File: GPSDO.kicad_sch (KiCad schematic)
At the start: 100 parts, among them J1 Conn_Coaxial, J10 Conn_Coaxial, J2 Barrel_Jack, J3 PROG, J4 DISP_MODULE, J5 GPS_CONN, J6 Conn_Coaxial, J7 Conn_Coaxial, J8 Conn_Coaxial, J9 Conn_Coaxial, SW1 RESET_BTN, U1 REF3450, U10 AVR32DB28x-xSO, U11 AZ1117H-5.0TRG1, U12 AZ1117H-5.0TRG1, U13 74HC390, U14 DS34C87T, U15 MCP6486T-E/OT, U2 74AUC2G04, U3 74AUC2G04, U4 74AUC1G74, U5 AD5680, U6 NB3N551MN, U7 74LVC1G125SE-7, U8 74LVC1G125SE-7, U9 LTC2050IS8, X1 OC5SC25

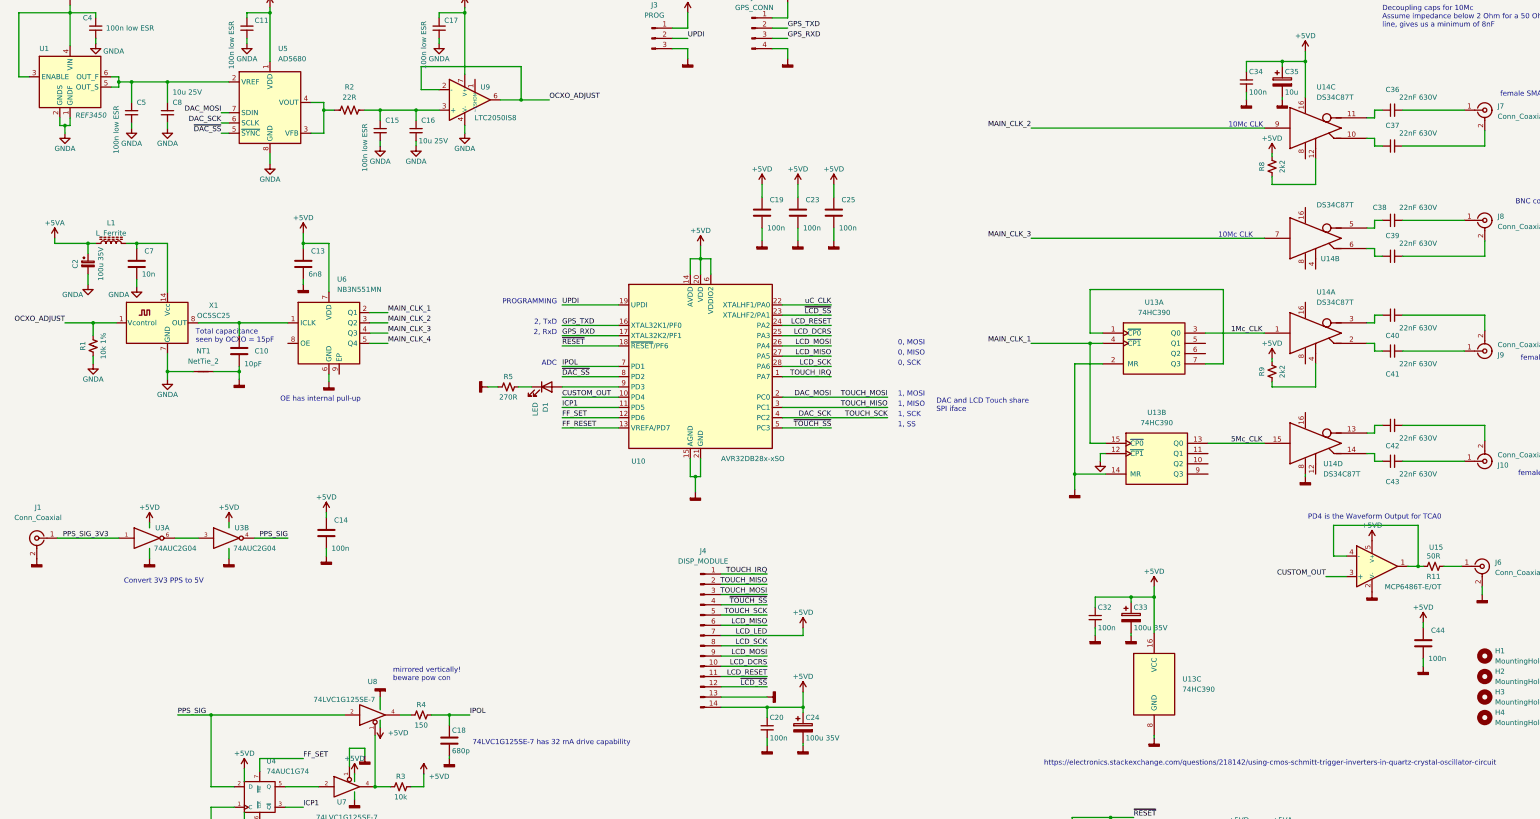
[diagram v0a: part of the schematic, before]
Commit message: Corrected schematic: VREF
VREF was chosen as 5V instead of 4.096V - corrected with REF3440IDBVR
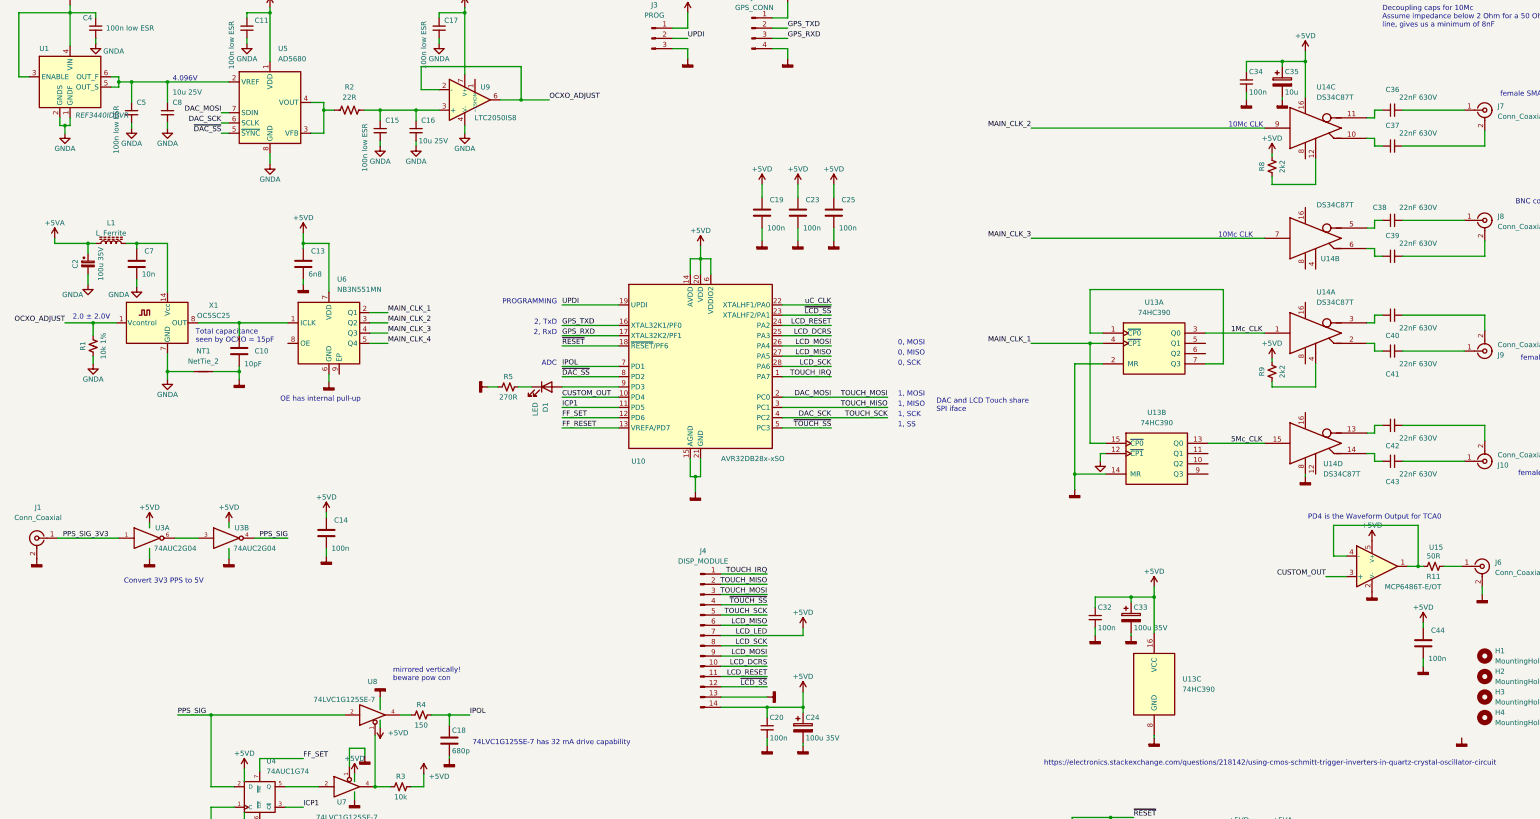
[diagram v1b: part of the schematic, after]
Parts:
- H1, H2, H3: footprint MountingHole:MountingHole_3.2mm_M3_Pad_Via -> MountingHole:MountingHole_3.2mm_M3_Pad
- U1: value REF3450 -> REF3440IDBVR
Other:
- note added: "2.0 ± 2.0V"
- note added: "4.096V"
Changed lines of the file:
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@@
     (effects (font (size 1.27 1.27)) (justify right bottom))
   )
+  (text "2.0 ± 2.0V" (at 29.845 97.79 0)
+    (effects (font (size 1.27 1.27)) (justify left bottom))
+  )
   (text "10Mc CLK" (at 316.23 50.165 0)
     (effects (font (size 1.27 1.27)) (justify left bottom))
@@
     (effects (font (size 1.27 1.27)) (justify left bottom))
   )
+  (text "4.096V" (at 54.61 38.735 0)
+    (effects (font (size 1.27 1.27)) (justify left bottom))
+  )
   (text "Total capacitance\nseen by OCXO = 15pF\n" (at 60.325 103.505 0)
     (effects (font (size 1.27 1.27)) (justify left bottom))
@@
     (pin "1")
   )
+  (symbol (lib_id "power:GNDD") (at 374.015 201.295 0) (unit 1)
+    (in_bom yes) (on_board yes) (fields_autoplaced)
+    (property "Reference" "#PWR0104" (id 0) (at 374.015 207.645 0)
+      (effects (font (size 1.27 1.27)) hide)
+    )
+    (property "Value" "GNDD" (id 1) (at 374.015 207.01 0)
+      (effects (font (size 1.27 1.27)) hide)
+    )
+    (property "Footprint" "" (id 2) (at 374.015 201.295 0)
+      (effects (font (size 1.27 1.27)) hide)
+    )
+    (property "Datasheet" "" (id 3) (at 374.015 201.295 0)
+      (effects (font (size 1.27 1.27)) hide)
+    )
+    (pin "1")
+  )
   (symbol (lib_id "74xGxx:74AUC1G125") (at 104.775 195.58 0) (mirror x) (unit 1)
     (in_bom yes) (on_board yes)
@@
       (effects (font (size 1.27 1.27)) (justify left))
     )
-    (property "Footprint" "MountingHole:MountingHole_3.2mm_M3_Pad_Via" (id 2) (at 379.73 180.975 0)
+    (property "Footprint" "MountingHole:MountingHole_3.2mm_M3_Pad" (id 2) (at 379.73 180.975 0)
       (effects (font (size 1.27 1.27)) hide)
     )
@@
       (effects (font (size 1.27 1.27)) (justify left))
     )
-    (property "Footprint" "MountingHole:MountingHole_3.2mm_M3_Pad_Via" (id 2) (at 379.73 186.055 0)
+    (property "Footprint" "MountingHole:MountingHole_3.2mm_M3_Pad" (id 2) (at 379.73 186.055 0)
       (effects (font (size 1.27 1.27)) hide)
     )
@@
       (effects (font (size 1.27 1.27)) (justify left))
     )
-    (property "Value" "REF3450" (id 1) (at 30.48 46.99 0)
+    (property "Value" "REF3440IDBVR" (id 1) (at 30.48 46.99 0)
       (effects (font (size 1.27 1.27) italic) (justify left))
     )
@@
       (effects (font (size 1.27 1.27)) (justify left))
     )
-    (property "Footprint" "MountingHole:MountingHole_3.2mm_M3_Pad_Via" (id 2) (at 379.73 191.135 0)
+    (property "Footprint" "MountingHole:MountingHole_3.2mm_M3_Pad" (id 2) (at 379.73 191.135 0)
       (effects (font (size 1.27 1.27)) hide)
     )
@@
       (reference "#PWR0103") (unit 1) (value "GNDD") (footprint "")
     )
+    (path "/38c92507-3a20-45d6-8807-152676b44109"
+      (reference "#PWR0104") (unit 1) (value "GNDD") (footprint "")
+    )
     (path "/8b6399fe-4a94-4985-af2b-54dc2c7e1be3"
       (reference "C1") (unit 1) (value "100u 35V") (footprint "Capacitor_SMD:C_Elec_6.3x7.7")
@@
     )
     (path "/66ef690a-322e-4ce3-ad31-6ee3e5fd6680"
-      (reference "H1") (unit 1) (value "MountingHole") (footprint "MountingHole:MountingHole_3.2mm_M3_Pad_Via")
+      (reference "H1") (unit 1) (value "MountingHole") (footprint "MountingHole:MountingHole_3.2mm_M3_Pad")
     )
     (path "/9edbda55-ac3d-4a3e-b128-bb0b0fdb9910"
-      (reference "H2") (unit 1) (value "MountingHole") (footprint "MountingHole:MountingHole_3.2mm_M3_Pad_Via")
+      (reference "H2") (unit 1) (value "MountingHole") (footprint "MountingHole:MountingHole_3.2mm_M3_Pad")
     )
     (path "/ebdbeddc-63be-4318-9a9c-af7712903058"
-      (reference "H3") (unit 1) (value "MountingHole") (footprint "MountingHole:MountingHole_3.2mm_M3_Pad_Via")
+      (reference "H3") (unit 1) (value "MountingHole") (footprint "MountingHole:MountingHole_3.2mm_M3_Pad")
     )
     (path "/9d53fc74-7a66-45cc-b056-4ff534da4a80"
@@
     )
     (path "/b4ee0a4b-62f3-44d8-a6db-f90e1929b0e8"
-      (reference "U1") (unit 1) (value "REF3450") (footprint "Package_TO_SOT_SMD:SOT-23-6")
+      (reference "U1") (unit 1) (value "REF3440IDBVR") (footprint "Package_TO_SOT_SMD:SOT-23-6")
     )
     (path "/0a178eb4-3897-49a1-913e-3a3d7dfb61f5"

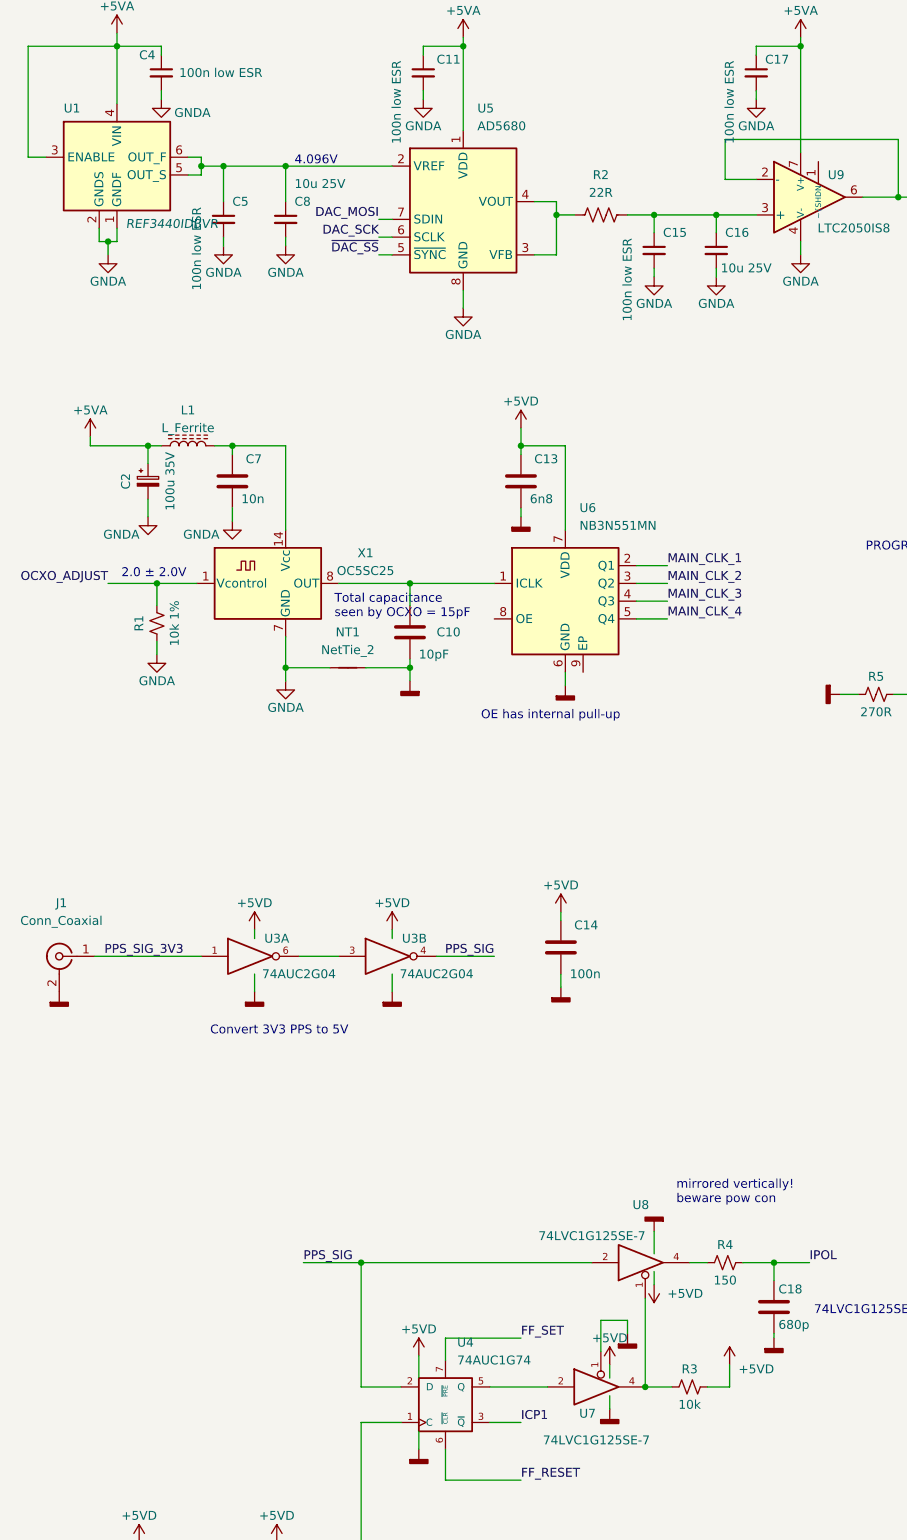
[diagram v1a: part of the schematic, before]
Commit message: Flip-flop error
Wrong device, wasn't 5V tolerant. Corrected
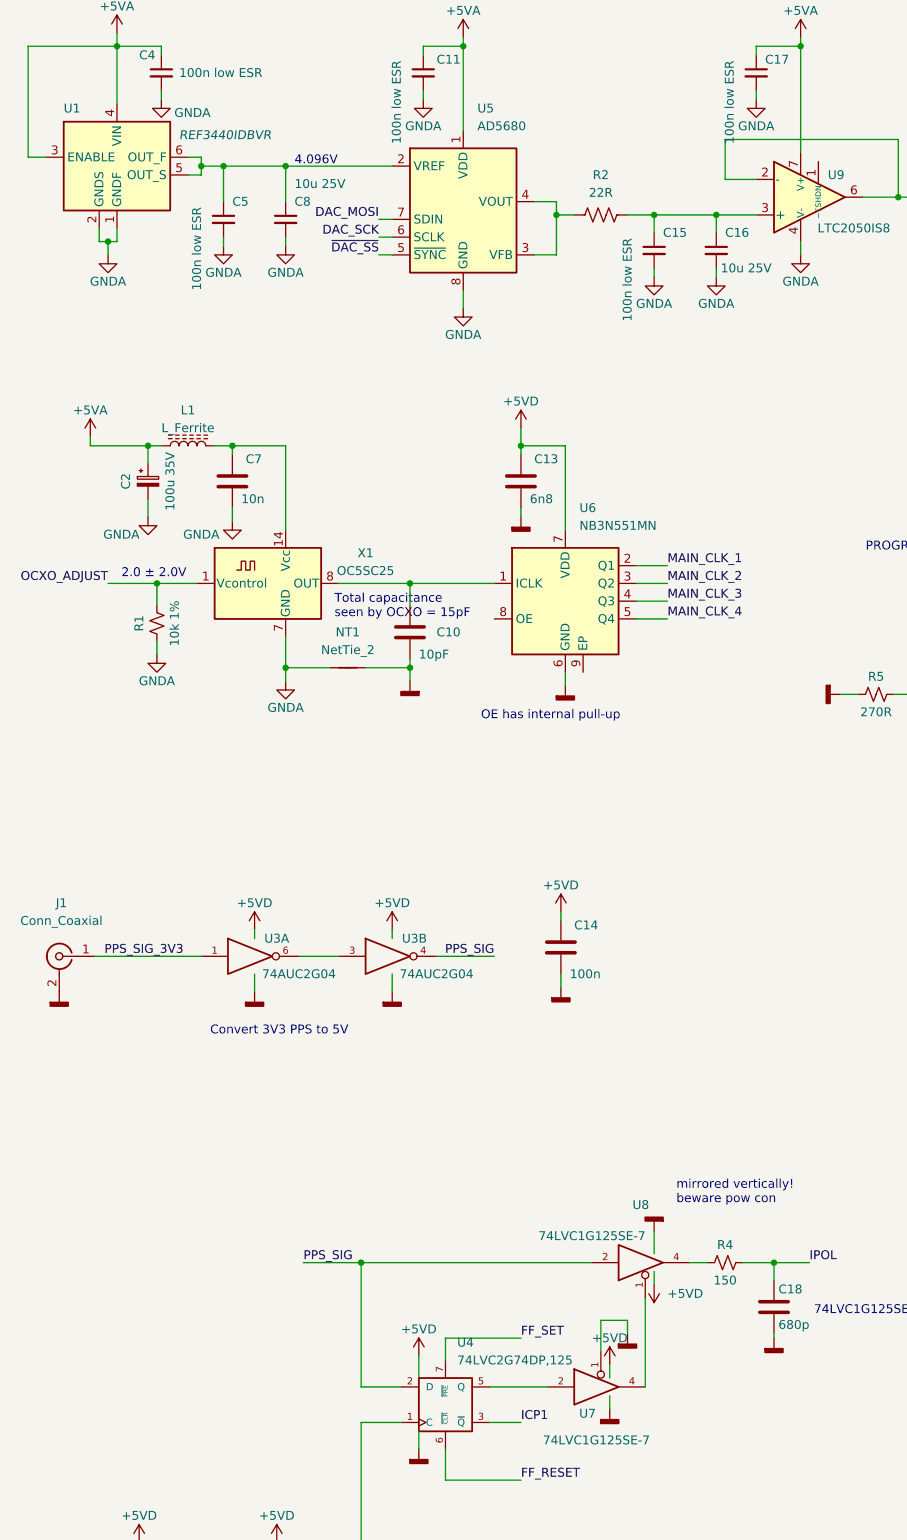
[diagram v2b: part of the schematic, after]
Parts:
- removed R3: 10k, Resistor_SMD:R_0805_2012Metric_Pad1.20x1.40mm_HandSolder, symbol Device:R_Small_US
- U4: value 74AUC1G74 -> 74LVC2G74DP,125; footprint Package_SO:VSSOP-8_2.3x2mm_P0.5mm -> Package_SO:TSSOP-8_3x3mm_P0.65mm
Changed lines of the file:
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@@
   (junction (at 120.65 269.24) (diameter 0) (color 0 0 0 0)
   )
-  (junction (at 104.775 213.36) (diameter 0) (color 0 0 0 0)
-  )
   (junction (at 227.33 234.95) (diameter 0) (color 0 0 0 0)
   )
@@
     (stroke (width 0) (type default) (color 0 0 0 0))
   )
-  (wire (pts (xy 116.84 210.185) (xy 116.84 213.36))
-    (stroke (width 0) (type default) (color 0 0 0 0))
-  )
   (wire (pts (xy 74.93 151.765) (xy 83.185 151.765))
     (stroke (width 0) (type default) (color 0 0 0 0))
@@
     (stroke (width 0) (type default) (color 0 0 0 0))
   )
-  (wire (pts (xy 108.585 213.36) (xy 104.775 213.36))
-    (stroke (width 0) (type default) (color 0 0 0 0))
-  )
   (wire (pts (xy 182.88 82.55) (xy 182.88 86.36))
     (stroke (width 0) (type default) (color 0 0 0 0))
@@
     (stroke (width 0) (type default) (color 0 0 0 0))
   )
-  (wire (pts (xy 116.84 213.36) (xy 113.665 213.36))
-    (stroke (width 0) (type default) (color 0 0 0 0))
-  )
   (wire (pts (xy 216.535 276.86) (xy 216.535 278.765))
     (stroke (width 0) (type default) (color 0 0 0 0))
@@
       (effects (font (size 1.27 1.27)) (justify left))
     )
-    (property "Value" "74AUC1G74" (id 1) (at 77.8701 209.55 0)
+    (property "Value" "74LVC2G74DP,125" (id 1) (at 77.8701 209.55 0)
       (effects (font (size 1.27 1.27)) (justify left))
     )
-    (property "Footprint" "Package_SO:VSSOP-8_2.3x2mm_P0.5mm" (id 2) (at 76.2 215.9 0)
+    (property "Footprint" "Package_SO:TSSOP-8_3x3mm_P0.65mm" (id 2) (at 76.2 215.9 0)
       (effects (font (size 1.27 1.27)) hide)
     )
@@
     (pin "2")
   )
-  (symbol (lib_id "Device:R_Small_US") (at 111.125 213.36 90) (unit 1)
-    (in_bom yes) (on_board yes)
-    (property "Reference" "R3" (id 0) (at 111.125 210.82 90))
-    (property "Value" "10k" (id 1) (at 111.125 215.9 90))
-    (property "Footprint" "Resistor_SMD:R_0805_2012Metric_Pad1.20x1.40mm_HandSolder" (id 2) (at 111.125 213.36 0)
-      (effects (font (size 1.27 1.27)) hide)
-    )
-    (property "Datasheet" "~" (id 3) (at 111.125 213.36 0)
-      (effects (font (size 1.27 1.27)) hide)
-    )
-    (pin "1")
-    (pin "2")
-  )
   (symbol (lib_id "74xx:74LS390") (at 297.815 103.505 0) (unit 1)
     (in_bom yes) (on_board yes) (fields_autoplaced)
@@
       (effects (font (size 1.27 1.27)) (justify left))
     )
-    (property "Value" "REF3440IDBVR" (id 1) (at 30.48 46.99 0)
+    (property "Value" "REF3440IDBVR" (id 1) (at 38.1 34.29 0)
       (effects (font (size 1.27 1.27) italic) (justify left))
     )
@@
     (pin "8")
   )
-  (symbol (lib_id "power:+5VD") (at 116.84 210.185 0) (unit 1)
-    (in_bom yes) (on_board yes)
-    (property "Reference" "#PWR048" (id 0) (at 116.84 213.995 0)
-      (effects (font (size 1.27 1.27)) hide)
-    )
-    (property "Value" "+5VD" (id 1) (at 118.11 210.82 0)
-      (effects (font (size 1.27 1.27)) (justify left))
-    )
-    (property "Footprint" "" (id 2) (at 116.84 210.185 0)
-      (effects (font (size 1.27 1.27)) hide)
-    )
-    (property "Datasheet" "" (id 3) (at 116.84 210.185 0)
-      (effects (font (size 1.27 1.27)) hide)
-    )
-    (pin "1")
-  )
   (symbol (lib_id "power:GNDD") (at 235.585 278.765 0) (unit 1)
     (in_bom yes) (on_board yes) (fields_autoplaced)
@@
       (reference "#PWR047") (unit 1) (value "GNDA") (footprint "")
     )
-    (path "/dc4a32ff-2cd1-4a27-9ccf-6829e740dd6d"
-      (reference "#PWR048") (unit 1) (value "+5VD") (footprint "")
-    )
     (path "/c3a20beb-54dd-40ec-98a4-c6e48b5d29d9"
       (reference "#PWR049") (unit 1) (value "GNDA") (footprint "")
@@
       (reference "R2") (unit 1) (value "22R") (footprint "Resistor_SMD:R_0805_2012Metric_Pad1.20x1.40mm_HandSolder")
     )
-    (path "/5a9dbd54-e88b-4b2a-8612-70685d2761b7"
-      (reference "R3") (unit 1) (value "10k") (footprint "Resistor_SMD:R_0805_2012Metric_Pad1.20x1.40mm_HandSolder")
-    )
     (path "/d36806d6-576f-484e-892a-2c51c9c2762a"
       (reference "R4") (unit 1) (value "150") (footprint "Resistor_SMD:R_0805_2012Metric_Pad1.20x1.40mm_HandSolder")
@@
     )
     (path "/14b7ea0b-a3fe-410e-b47a-552eaf1c5ffd"
-      (reference "U4") (unit 1) (value "74AUC1G74") (footprint "Package_SO:VSSOP-8_2.3x2mm_P0.5mm")
+      (reference "U4") (unit 1) (value "74LVC2G74DP,125") (footprint "Package_SO:TSSOP-8_3x3mm_P0.65mm")
     )
     (path "/b762cdfa-b658-4216-93f0-a3e3f1ba8c89"
